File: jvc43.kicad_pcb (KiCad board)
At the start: 6 copper layers, 101.6 x 50.8 mm, 119 parts, among them J201 8P8C_LED_Shielded, J301 8P8C_LED_Shielded, J401 USB_C_Receptacle_USB2.0, U201 LAN8810, U301 LAN8810, U401 LTC3622*DE, X101 25 MHz

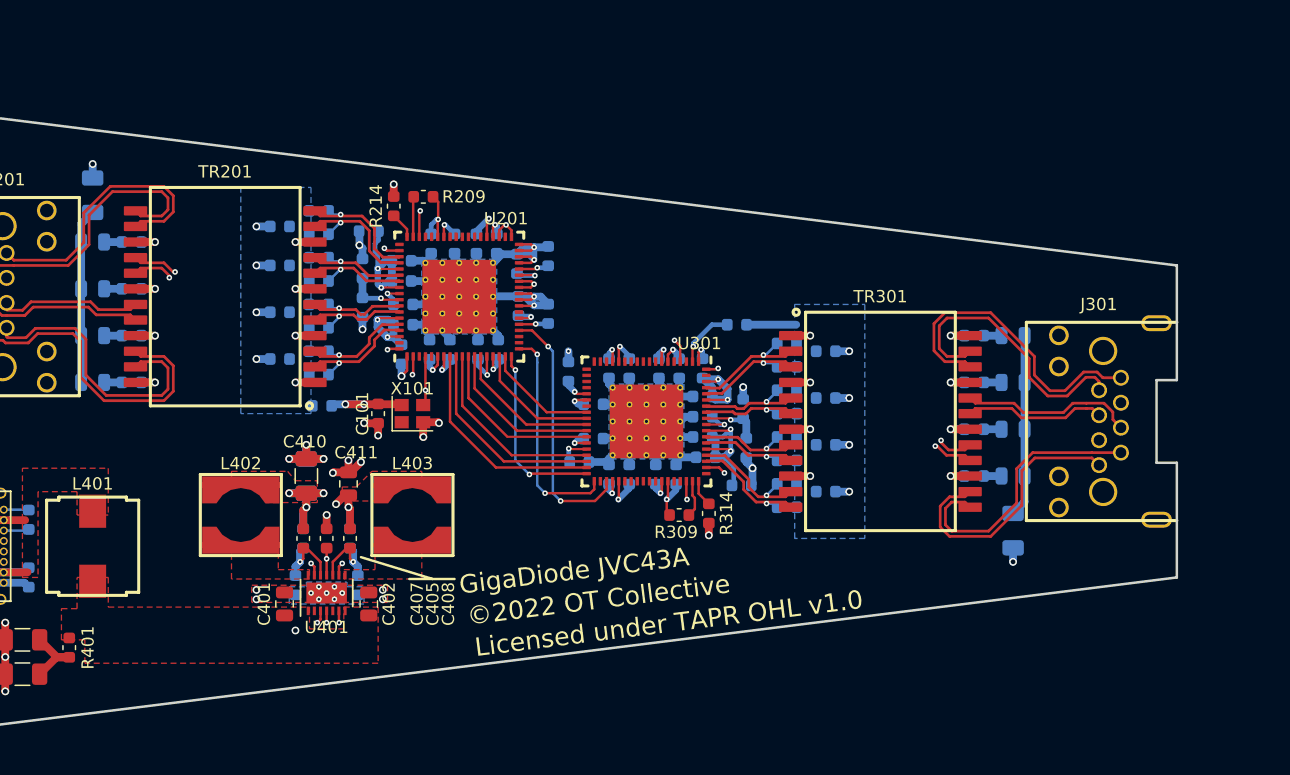
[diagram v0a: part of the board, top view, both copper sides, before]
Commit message: - Added HPD_MODE strap resistor - Narrowed down from an RJ45 family P/N to a very specific P/N - Added RJ45 LED hookups - Added CONFIG0/1/2/3 hookups, including a bunch of 0402 zero-ohm options - Placed and routed all of the above except the LED resistors/traces
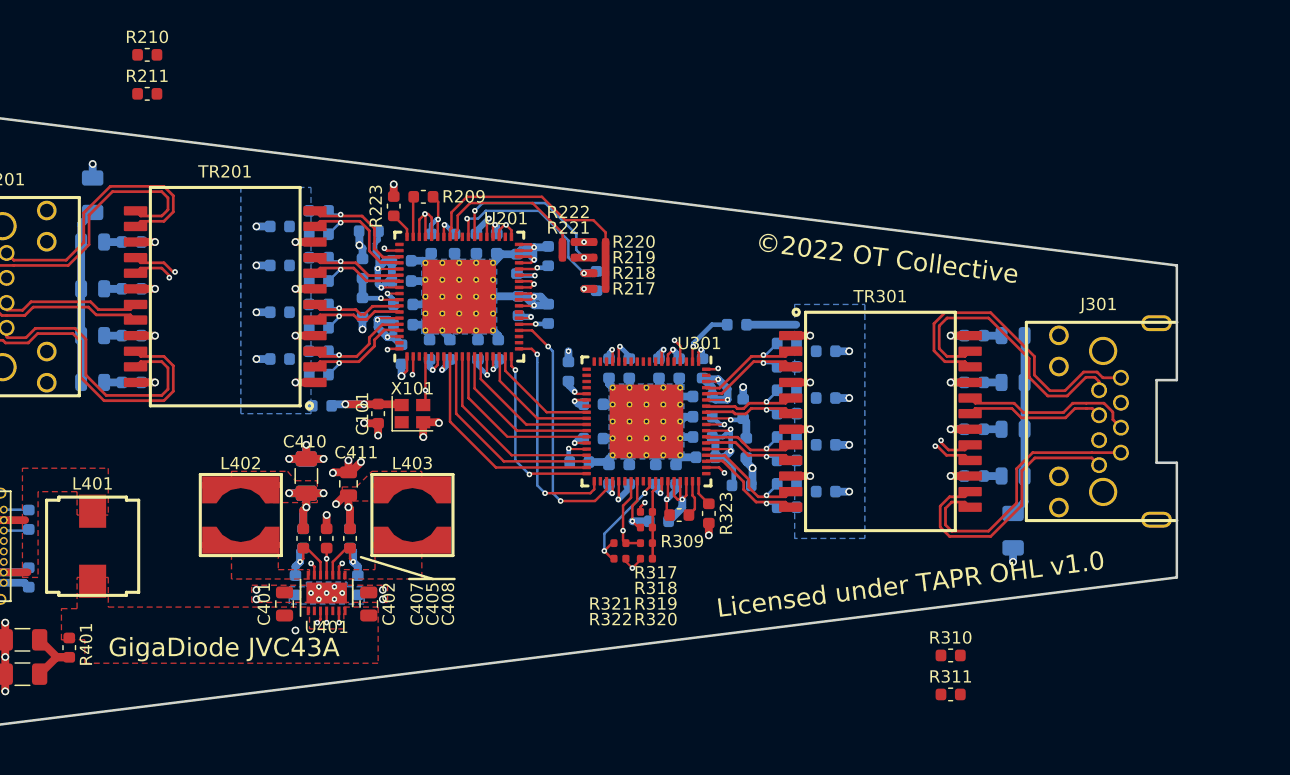
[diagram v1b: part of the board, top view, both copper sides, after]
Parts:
- added R210: 100, Resistor_SMD:R_0603_1608Metric, F.Cu at (43.2, 21.0)
- added R211: 100, Resistor_SMD:R_0603_1608Metric, F.Cu at (43.2, 24.1)
- added R216: 5k1, Resistor_SMD:R_0603_1608Metric, B.Cu at (79.8, 39.4)
- added R217: 0, Resistor_SMD:R_0402_1005Metric, F.Cu at (80.0, 40.0)
- added R218: dnp, Resistor_SMD:R_0402_1005Metric, F.Cu at (80.0, 38.7)
- added R219: dnp, Resistor_SMD:R_0402_1005Metric, F.Cu at (80.0, 37.5)
- added R220: dnp, Resistor_SMD:R_0402_1005Metric, F.Cu at (80.0, 36.2)
- added R221: dnp, Resistor_SMD:R_0402_1005Metric, F.Cu at (77.5, 37.5)
- added R222: 0, Resistor_SMD:R_0402_1005Metric, F.Cu at (77.5, 36.2)
- added R310: 100, Resistor_SMD:R_0603_1608Metric, F.Cu at (108.6, 69.8)
- added R311: 100, Resistor_SMD:R_0603_1608Metric, F.Cu at (108.6, 73.0)
- added R316: 5k1, Resistor_SMD:R_0603_1608Metric, B.Cu at (84.8, 58.9)
- added R317: 0, Resistor_SMD:R_0402_1005Metric, F.Cu at (83.8, 58.2)
- added R318: dnp, Resistor_SMD:R_0402_1005Metric, F.Cu at (83.8, 59.4)
- added R319: dnp, Resistor_SMD:R_0402_1005Metric, F.Cu at (83.8, 60.7)
- added R320: dnp, Resistor_SMD:R_0402_1005Metric, F.Cu at (83.8, 62.0)
- added R321: dnp, Resistor_SMD:R_0402_1005Metric, F.Cu at (81.7, 60.7)
- added R322: 0, Resistor_SMD:R_0402_1005Metric, F.Cu at (81.7, 62.0)
- renumbered C202 to C201, C203 to C202, C204 to C203, C205 to C204, C206 to C205, C207 to C206, C208 to C207, C209 to C208, C210 to C209, C211 to C210, C212 to C211, C213 to C212, C214 to C213, C215 to C214, C216 to C215, C217 to C216, C218 to C217, C219 to C218, C220 to C219, C221 to C220, C222 to C221, C223 to C222, C224 to C223, C225 to C224, C226 to C225, C227 to C226, C228 to C227, C302 to C301, C303 to C302, C304 to C303, C305 to C304, C306 to C305, C307 to C306, C308 to C307, C309 to C308, C310 to C309, C311 to C310, C312 to C311, C313 to C312, C314 to C313, C315 to C314, C316 to C315, C317 to C316, C318 to C317, C319 to C318, C320 to C319, C321 to C320, C322 to C321, C323 to C322, C324 to C323, C325 to C324, C326 to C325, C327 to C326, C328 to C327, R210 to R212, R211 to R213, R212 to R214, R213 to R215, R214 to R223, R310 to R312, R311 to R313, R312 to R314, R313 to R315, R314 to R323
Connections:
- J201 pad 10: Net-(J201-Pad10) -> GND
- J201 pad 11: Net-(J201-Pad11) -> /Ethernet1/yellow
- J201 pad 12: Net-(J201-Pad12) -> GND
- J201 pad 9: Net-(J201-Pad9) -> /Ethernet1/green
- J301 pad 10: Net-(J301-Pad10) -> GND
- J301 pad 11: Net-(J301-Pad11) -> /Ethernet2/yellow
- J301 pad 12: Net-(J301-Pad12) -> GND
- J301 pad 9: Net-(J301-Pad9) -> /Ethernet2/green
- U201 pad 50: /Ethernet1/CONFIG1 -> GND
- U201 pad 51: /Ethernet1/CONFIG0 -> GND
- U301 pad 50: /Ethernet2/CONFIG1 -> GND
- U301 pad 51: /Ethernet2/CONFIG0 -> GND
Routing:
- net /Ethernet1/CONFIG2: track 0.00 -> 20.9 mm
- net /Ethernet1/100_LED: track 0.00 -> 16.1 mm, vias 0 -> 2
- net /Ethernet1/1000_LED: track 0.00 -> 15.4 mm, vias 0 -> 2
- net /Ethernet1/CONFIG3: track 0.00 -> 13.8 mm
- net GND: track 113.1 -> 125.8 mm, vias 52 -> 54
- net /Ethernet2/CONFIG3: track 0.00 -> 9.29 mm, vias 0 -> 2
- net /Ethernet2/1000_LED: track 0.00 -> 6.59 mm, vias 0 -> 1
- net /Ethernet2/CONFIG2: track 0.00 -> 6.42 mm
- net /Ethernet2/100_LED: track 0.00 -> 5.66 mm, vias 0 -> 1
- net +2V5: track 56.9 -> 60.5 mm, vias 20 -> 22

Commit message: Added an identifier to the back silkscreen
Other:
- board text added: "0192 7494 9C16 FF49 264F 2293 A298 2C77 3C0B 4DAD"
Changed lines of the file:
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@@
   (general
     (thickness 1.6002)
-    (drawings 38)
+    (drawings 39)
     (tracks 1158)
     (zones 0)
@@
     )
   )
+  (gr_text "0192 7494 9C16 FF49 264F\n2293 A298 2C77 3C0B 4DAD" (at 104.775 50.8 90) (layer B.SilkS)
+    (effects (font (size 1.27 1.27) (thickness 0.254)) (justify mirror))
+  )
   (gr_text "Licensed under TAPR OHL v1.0" (at 89.535 66.04 7.1) (layer F.SilkS)
     (effects (font (size 1.5 1.5) (thickness 0.3)) (justify left))
@@
   (gr_line (start 25.4 76.2) (end 25.4 44.0055) (layer Edge.Cuts) (width 0.2032))
   (gr_line (start 25.4 25.4) (end 127 38.1) (layer Edge.Cuts) (width 0.2032))
-  (via (at 78.74 36.195) (size 0.4572) (drill 0.2032) (layers F.Cu B.Cu) (net 102))
-  (via (at 82.677 62.738) (size 0.4572) (drill 0.2032) (layers F.Cu B.Cu) (net 102))
-  (via (at 80.391 61.341) (size 0.4572) (drill 0.2032) (layers F.Cu B.Cu) (net 122))
   (via (at 58.42 65.278) (size 0.4572) (drill 0.2032) (layers F.Cu B.Cu) (net 1))
   (via (at 58.42 64.262) (size 0.4572) (drill 0.2032) (layers F.Cu B.Cu) (net 1))
@@
   (segment (start 76.835 57.277) (end 76.2 56.642) (width 0.2032) (layer B.Cu) (net 66))
   (segment (start 76.2 56.642) (end 76.2 45.085) (width 0.2032) (layer B.Cu) (net 66))
-  (segment (start 41.1225 36.195) (end 39.6725 36.195) (width 0.635) (layer B.Cu) (net 134))
   (segment (start 41.1225 40.005) (end 39.6725 40.005) (width 0.635) (layer B.Cu) (net 67))
   (segment (start 41.1225 43.815) (end 39.6725 43.815) (width 0.635) (layer B.Cu) (net 68))
@@
   (via (at 38.735 29.845) (size 0.635) (drill 0.381) (layers F.Cu B.Cu) (net 70))
   (segment (start 38.735 30.985) (end 38.735 29.845) (width 0.635) (layer B.Cu) (net 70))
-  (segment (start 111.2775 55.245) (end 112.7275 55.245) (width 0.635) (layer B.Cu) (net 135))
   (segment (start 111.2775 51.435) (end 112.7275 51.435) (width 0.635) (layer B.Cu) (net 71))
   (segment (start 111.2775 47.625) (end 112.7275 47.625) (width 0.635) (layer B.Cu) (net 72))
@@
   (segment (start 60.325 62.611) (end 59.944 62.23) (width 0.635) (layer B.Cu) (net 101))
   (segment (start 60.325 63.3475) (end 60.325 62.611) (width 0.635) (layer B.Cu) (net 101))
+  (via (at 78.74 36.195) (size 0.4572) (drill 0.2032) (layers F.Cu B.Cu) (net 102))
+  (via (at 82.677 62.738) (size 0.4572) (drill 0.2032) (layers F.Cu B.Cu) (net 102))
   (via (at 74.803 42.8625) (size 0.4572) (drill 0.2032) (layers F.Cu B.Cu) (net 102))
   (segment (start 73.45 42.89) (end 74.7755 42.89) (width 0.2032) (layer F.Cu) (net 102))
@@
   (segment (start 83.335 59.436) (end 83.185 59.436) (width 0.2032) (layer F.Cu) (net 120))
   (segment (start 82.677 58.928) (end 84.0485 58.928) (width 0.635) (layer B.Cu) (net 120))
+  (via (at 80.391 61.341) (size 0.4572) (drill 0.2032) (layers F.Cu B.Cu) (net 122))
   (segment (start 84.07 55.67) (end 84.07 56.138) (width 0.2032) (layer F.Cu) (net 122))
   (via (at 83.693 56.642) (size 0.4572) (drill 0.2032) (layers F.Cu B.Cu) (net 122))
@@
   (segment (start 84.328 61.953) (end 84.305 61.976) (width 0.2032) (layer F.Cu) (net 123))
   (segment (start 84.328 56.515) (end 84.328 61.953) (width 0.2032) (layer F.Cu) (net 123))
+  (segment (start 41.1225 36.195) (end 39.6725 36.195) (width 0.635) (layer B.Cu) (net 134))
+  (segment (start 111.2775 55.245) (end 112.7275 55.245) (width 0.635) (layer B.Cu) (net 135))
   (zone (net 70) (net_name /Ethernet1/gnd_eth) (layer L2.Cu) (hatch edge 0.508)
     (connect_pads (clearance 0.254))

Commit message: Updated the title blocks / naming
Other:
- board text added: "BACK COPPER"
- board text added: "BACK FAB"
- board text added: "BACK SILKSCREEN"
- board text added: "BACK SOLDERMASK"
- board text added: "BACK SOLDERPASTE"
- board text added: "FRONT COPPER"
- board text added: "FRONT FAB"
- board text added: "FRONT SILKSCREEN"
- board text added: "FRONT SOLDERMASK"
- board text added: "FRONT SOLDERPASTE"
- board text added: "L2 COPPER"
- board text added: "L3 COPPER"
- board text added: "L4 COPPER"
- board text added: "L5 COPPER"
- board text added: "©2022 OT Conclave"
- board text removed: "JVC34A BACK COPPER"
- board text removed: "JVC34A BACK FAB"
- board text removed: "JVC34A BACK SILKSCREEN"
- board text removed: "JVC34A BACK SOLDERMASK"
- board text removed: "JVC34A BACK SOLDERPASTE"
- board text removed: "JVC34A FRONT COPPER"
- board text removed: "JVC34A FRONT FAB"
- board text removed: "JVC34A FRONT SILKSCREEN"
- board text removed: "JVC34A FRONT SOLDERMASK"
- board text removed: "JVC34A FRONT SOLDERPASTE"
- board text removed: "JVC34A L2 COPPER"
- board text removed: "JVC34A L3 COPPER"
- board text removed: "JVC34A L4 COPPER"
- board text removed: "JVC34A L5 COPPER"
- board text removed: "©2022 OT Collective"
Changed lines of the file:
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@@
   (page B)
   (title_block
-    (title JVC43A)
-    (date 2022-12-07)
+    (title "GigaDiode / JVC43A")
+    (date 2022-12-09)
     (rev 1)
-    (company "©2022 OT Collective")
+    (company "©2022 OT Conclave")
     (comment 1 "Licensed under the TAPR Open Hardware License v1.0")
   )
@@
     (effects (font (size 1.5 1.5) (thickness 0.3)) (justify left))
   )
-  (gr_text "©2022 OT Collective" (at 92.71 36.195 -7.1) (layer F.SilkS)
+  (gr_text "©2022 OT Conclave" (at 92.71 36.195 -7.1) (layer F.SilkS)
     (effects (font (size 1.5 1.5) (thickness 0.3)) (justify left))
   )
@@
   (gr_line (start 27.051 44.0055) (end 27.051 37.2745) (layer Edge.Cuts) (width 0.2032))
   (gr_line (start 25.4 44.0055) (end 27.051 44.0055) (layer Edge.Cuts) (width 0.2032))
-  (gr_text "JVC34A L5 COPPER" (at 330.2 187.96) (layer L5.Cu)
+  (gr_text "L5 COPPER" (at 330.2 187.96) (layer L5.Cu)
     (effects (font (size 1.5 1.5) (thickness 0.3)) (justify left))
   )
-  (gr_text "JVC34A L4 COPPER" (at 330.2 185.42) (layer L4.Cu)
+  (gr_text "L4 COPPER" (at 330.2 185.42) (layer L4.Cu)
     (effects (font (size 1.5 1.5) (thickness 0.3)) (justify left))
   )
-  (gr_text "JVC34A L3 COPPER" (at 330.2 182.88) (layer L3.Cu)
+  (gr_text "L3 COPPER" (at 330.2 182.88) (layer L3.Cu)
     (effects (font (size 1.5 1.5) (thickness 0.3)) (justify left))
   )
-  (gr_text "JVC34A L2 COPPER" (at 330.2 180.34) (layer L2.Cu)
+  (gr_text "L2 COPPER" (at 330.2 180.34) (layer L2.Cu)
     (effects (font (size 1.5 1.5) (thickness 0.3)) (justify left))
   )
-  (gr_text "JVC34A BACK FAB" (at 330.2 210.82) (layer B.Fab)
+  (gr_text "BACK FAB" (at 330.2 210.82) (layer B.Fab)
     (effects (font (size 1.5 1.5) (thickness 0.3)) (justify left))
   )
-  (gr_text "JVC34A FRONT FAB" (at 330.2 208.28) (layer F.Fab)
+  (gr_text "FRONT FAB" (at 330.2 208.28) (layer F.Fab)
     (effects (font (size 1.5 1.5) (thickness 0.3)) (justify left))
   )
-  (gr_text "JVC34A BACK SOLDERMASK" (at 330.2 205.74) (layer B.Mask)
+  (gr_text "BACK SOLDERMASK" (at 330.2 205.74) (layer B.Mask)
     (effects (font (size 1.5 1.5) (thickness 0.3)) (justify left))
   )
-  (gr_text "JVC34A FRONT SOLDERMASK" (at 330.2 203.2) (layer F.Mask)
+  (gr_text "FRONT SOLDERMASK" (at 330.2 203.2) (layer F.Mask)
     (effects (font (size 1.5 1.5) (thickness 0.3)) (justify left))
   )
-  (gr_text "JVC34A BACK SILKSCREEN" (at 330.2 200.66) (layer B.SilkS)
+  (gr_text "BACK SILKSCREEN" (at 330.2 200.66) (layer B.SilkS)
     (effects (font (size 1.5 1.5) (thickness 0.3)) (justify left))
   )
-  (gr_text "JVC34A FRONT SILKSCREEN" (at 330.2 198.12) (layer F.SilkS)
+  (gr_text "FRONT SILKSCREEN" (at 330.2 198.12) (layer F.SilkS)
     (effects (font (size 1.5 1.5) (thickness 0.3)) (justify left))
   )
-  (gr_text "JVC34A BACK SOLDERPASTE" (at 330.2 195.58) (layer B.Paste)
+  (gr_text "BACK SOLDERPASTE" (at 330.2 195.58) (layer B.Paste)
     (effects (font (size 1.5 1.5) (thickness 0.3)) (justify left))
   )
-  (gr_text "JVC34A FRONT SOLDERPASTE" (at 330.2 193.04) (layer F.Paste)
+  (gr_text "FRONT SOLDERPASTE" (at 330.2 193.04) (layer F.Paste)
     (effects (font (size 1.5 1.5) (thickness 0.3)) (justify left))
   )
-  (gr_text "JVC34A BACK COPPER" (at 330.2 190.5) (layer B.Cu)
+  (gr_text "BACK COPPER" (at 330.2 190.5) (layer B.Cu)
     (effects (font (size 1.5 1.5) (thickness 0.3)) (justify left))
   )
-  (gr_text "JVC34A FRONT COPPER" (at 330.2 177.8) (layer F.Cu)
+  (gr_text "FRONT COPPER" (at 330.2 177.8) (layer F.Cu)
     (effects (font (size 1.5 1.5) (thickness 0.3)) (justify left))
   )

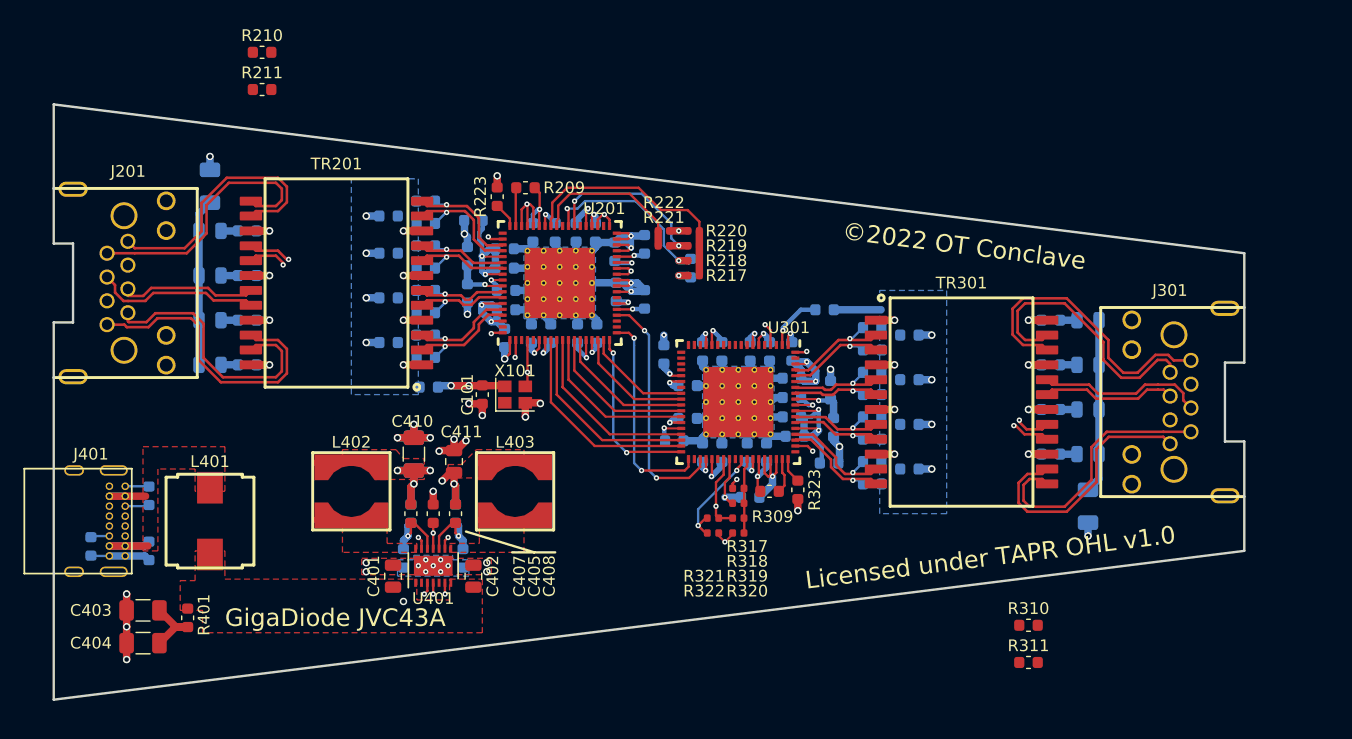
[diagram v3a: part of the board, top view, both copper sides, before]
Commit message: - Placed and routed the LED resistors & lines - This involved tweaking the 2kV Ethernet capacitor a bit - Also moved some front silkscreen refdes & major board texts
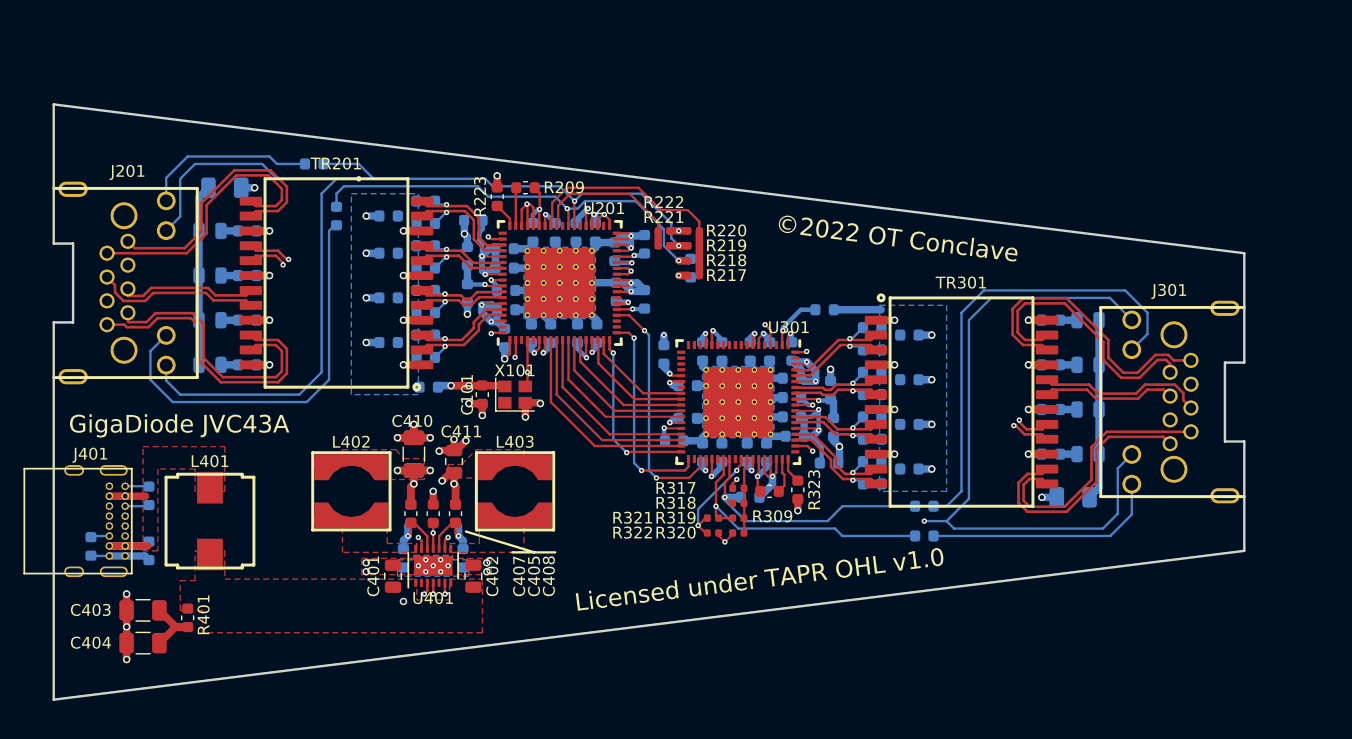
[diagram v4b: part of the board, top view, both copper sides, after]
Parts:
- R210, R211, R310, R311: moved to B.Cu
- moved R210 15.3 mm to (49.5, 34.9), turned to 270 degrees
- moved R311 14.0 mm to (99.7, 62.2)
- moved R310 13.5 mm to (99.7, 59.7)
- moved R211 7.75 mm to (47.6, 30.5), turned to 180 degrees
- moved C309 1.48 mm to (112.4, 58.9), turned to 180 degrees
- moved C209 1.28 mm to (40.0, 32.5), turned to 0 degrees
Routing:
- net GND: track 125.8 -> 236.1 mm, vias 54 -> 56
- net /Ethernet2/yellow: track 0.00 -> 39.3 mm
- net /Ethernet1/yellow: track 0.00 -> 34.7 mm
- net /Ethernet1/1000_LED: track 15.4 -> 38.2 mm
- net /Ethernet1/100_LED: track 16.1 -> 38.0 mm
- net /Ethernet2/green: track 0.00 -> 20.3 mm
- net /Ethernet2/1000_LED: track 6.59 -> 24.6 mm
- net /Ethernet2/100_LED: track 5.66 -> 23.4 mm
- net /Ethernet1/green: track 0.00 -> 14.8 mm
- net /Ethernet1/eth_inter_gnd: track 14.2 -> 15.4 mm
- net /Ethernet2/eth_inter_gnd: track 14.9 -> 15.4 mm
- net /Ethernet1/ETH_TX0-: track 23.0 -> 23.6 mm
- net /Ethernet1/ETH_TX0+: track 22.9 -> 23.4 mm
